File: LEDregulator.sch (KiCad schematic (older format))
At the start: 34 parts, among them J1 2.1mm DC jack, J2 2way Screw Terminal, J3 2way Screw Terminal, SW1 DPDT Switch, SW2 6pos rotary

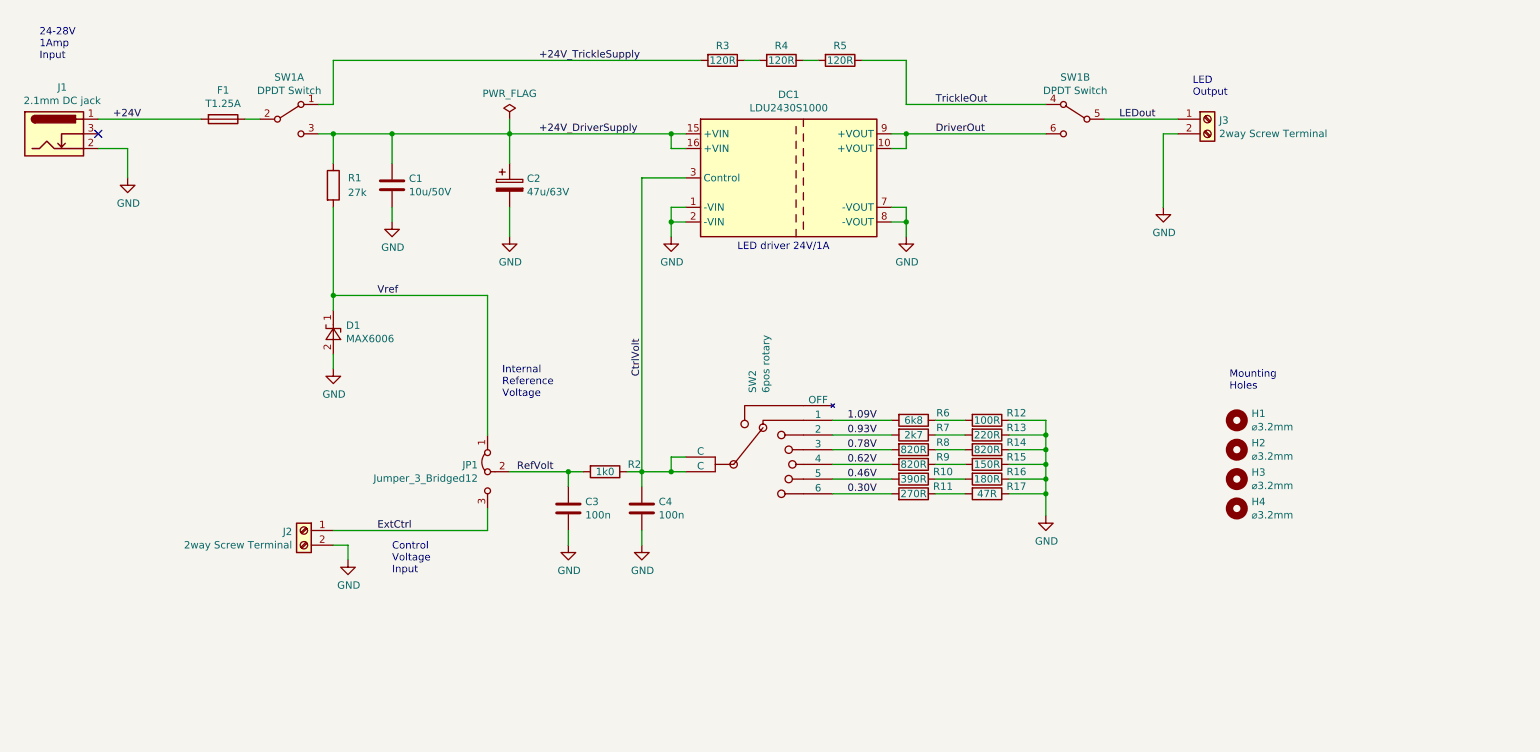
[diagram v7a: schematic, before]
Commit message: Started a new branch (v1.1) that has got fan control, low-side switch on the LED for trickle current and power resistors. Also the 5.08mm terminal connectors have been changed to more compact 3.81mm.
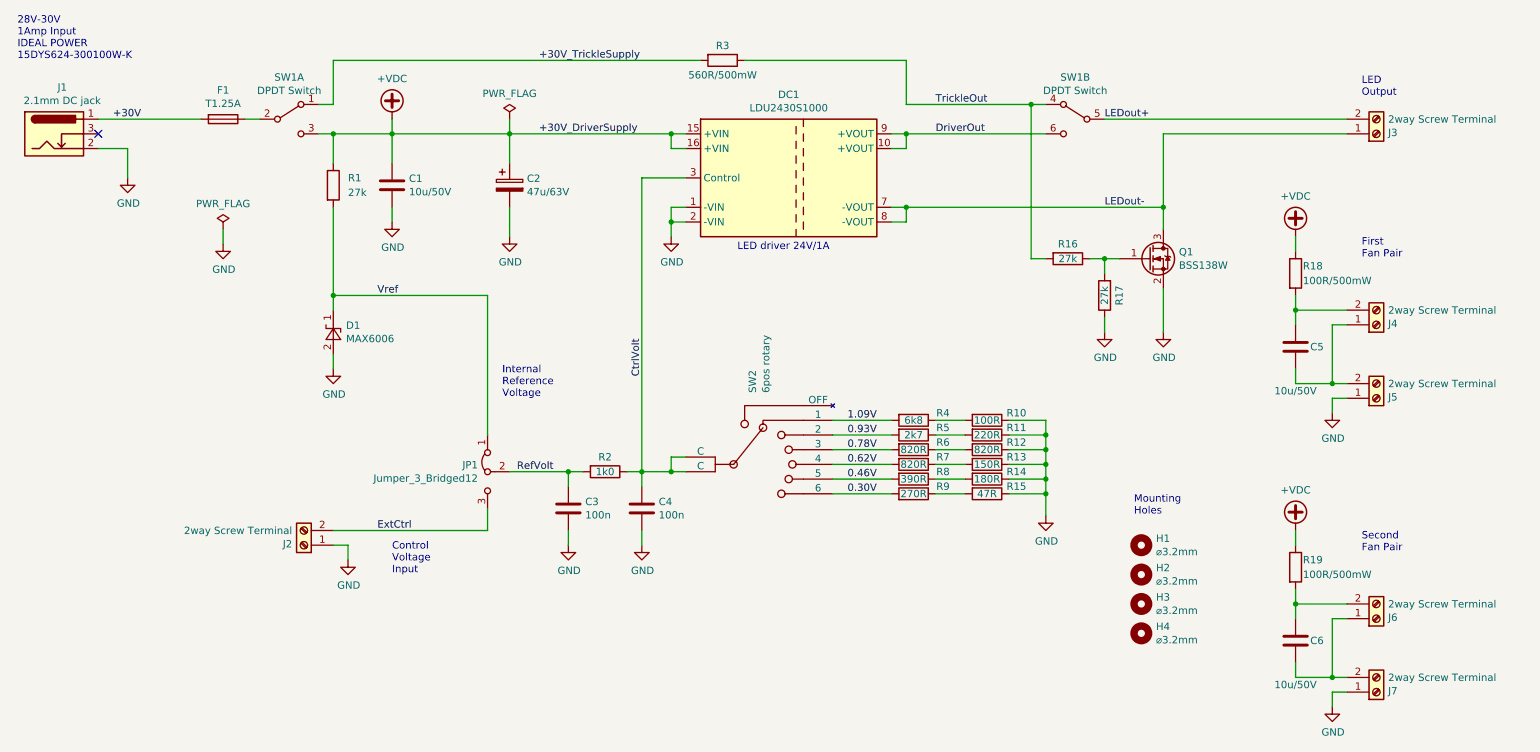
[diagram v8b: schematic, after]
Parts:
- removed R4, R5: 120R, Resistors_SMD:R_0603, symbol Device:R
- added C5, C6: 10u/50V, Capacitor_SMD:C_1206_3216Metric, symbol Device:C
- added J4, J5, J6, J7: 2way Screw Terminal, TerminalBlock_MetzConnect:TerminalBlock_MetzConnect_Type086_RT03402HBLC_1x02_P3.81mm_Horizontal, symbol Connector:Screw_Terminal_01x02
- added Q1: BSS138W, Package_TO_SOT_SMD:SOT-23, symbol Device:Q_NMOS_GSD
- added R16, R17: 27k, Resistor_SMD:R_0603_1608Metric, symbol Device:R
- added R18, R19: 100R/500mW, Resistor_SMD:R_1206_3216Metric_Pad1.42x1.75mm_HandSolder, symbol Device:R
- C1: footprint Capacitors_SMD:C_1206 -> Capacitor_SMD:C_1206_3216Metric
- C3, C4: footprint Capacitors_SMD:C_0603 -> Capacitor_SMD:C_0603_1608Metric
- J2, J3: footprint Terminal_Blocks:TerminalBlock_bornier-2_P5.08mm -> TerminalBlock_MetzConnect:TerminalBlock_MetzConnect_Type086_RT03402HBLC_1x02_P3.81mm_Horizontal; Description 2way 5.08mm screw terminal -> 2way 3.81mm screw terminal; Order Code 2008004 -> 2007985; Part Number MC000034 -> MC000018
- R1, R2: footprint Resistors_SMD:R_0603 -> Resistor_SMD:R_0603_1608Metric
- R10: renamed from R12; footprint Resistors_SMD:R_0603 -> Resistor_SMD:R_0603_1608Metric
- R11: renamed from R13; footprint Resistors_SMD:R_0603 -> Resistor_SMD:R_0603_1608Metric
- R12: renamed from R14; footprint Resistors_SMD:R_0603 -> Resistor_SMD:R_0603_1608Metric
- R13: renamed from R15; footprint Resistors_SMD:R_0603 -> Resistor_SMD:R_0603_1608Metric
- R14: renamed from R16; footprint Resistors_SMD:R_0603 -> Resistor_SMD:R_0603_1608Metric
- R15: renamed from R17; footprint Resistors_SMD:R_0603 -> Resistor_SMD:R_0603_1608Metric
- R3: value 120R -> 560R/500mW; footprint Resistors_SMD:R_0603 -> Resistor_SMD:R_1206_3216Metric_Pad1.42x1.75mm_HandSolder; Description 120Ω 0603 1% SMD resistor -> 560Ω 1206 1% 500mW SMD resistor; Manufacturer Multicomp -> TE Connectivity; Order Code 2447240 -> 2332136; Part Number MCWR06X1500FTL -> CRGH1206F560R
- R4: renamed from R6; footprint Resistors_SMD:R_0603 -> Resistor_SMD:R_0603_1608Metric
- R5: renamed from R7; footprint Resistors_SMD:R_0603 -> Resistor_SMD:R_0603_1608Metric
- R6: renamed from R8; footprint Resistors_SMD:R_0603 -> Resistor_SMD:R_0603_1608Metric
- R7: renamed from R9; footprint Resistors_SMD:R_0603 -> Resistor_SMD:R_0603_1608Metric
- R8: renamed from R10; footprint Resistors_SMD:R_0603 -> Resistor_SMD:R_0603_1608Metric
- R9: renamed from R11; footprint Resistors_SMD:R_0603 -> Resistor_SMD:R_0603_1608Metric
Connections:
- net ExtCtrl: now also J2.2 (Pin_2); no longer J2.1 (Pin_1)
- net GND: now also J2.1 (Pin_1), J5.1 (Pin_1), J7.1 (Pin_1), Q1.2 (S), R17.1; no longer DC1.7 (-VOUT), DC1.8 (-VOUT), J2.2 (Pin_2), J3.2 (Pin_2)
- net TrickleOut: now also R3.1, R16.2
- net +24V renamed +30V
- net +24V_DriverSupply renamed +VDC
- net +VDC: now also R18.1, R19.1
- net +24V_TrickleSupply renamed +30V_TrickleSupply
- net LEDout renamed LEDout+
- net LEDout+: now also J3.2 (Pin_2); no longer J3.1 (Pin_1)
- new net: Q1.1 (G), R16.1, R17.2
- new net: C5.2, J4.1 (Pin_1), J5.2 (Pin_2)
- new net: C5.1, J4.2 (Pin_2), R18.2
- new net: C6.2, J6.1 (Pin_1), J7.2 (Pin_2)
- new net: C6.1, J6.2 (Pin_2), R19.2
- new net LEDout-: DC1.7 (-VOUT), DC1.8 (-VOUT), J3.1 (Pin_1), Q1.3 (D)
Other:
- note added: "28V-30V\n1Amp Input\nIDEAL POWER \n15DYS624-300100W-K"
- note added: "First\nFan Pair"
- note added: "Second\nFan Pair"
- note removed: "24-28V\n1Amp\nInput"
- moved on the sheet: H1, H2, H3, H4, J3
